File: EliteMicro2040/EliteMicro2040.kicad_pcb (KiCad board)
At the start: 2 copper layers, 17.8 x 30.5 mm, 39 parts, among them J2 B3U, U1 SPX3819M5-L-3-3, U2 Elite-C, U3 RP2040, U4 W25Q32JVSS, Y1 3225_4P

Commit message: small tweaks + generated gerbers
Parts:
- moved C2 0.37 mm to (36.1, 51.6)
- moved C1 0.22 mm to (44.4, 33.5)
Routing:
- net +3V3: track 32.2 -> 29.4 mm
- net /SWD: track 2.22 -> 0.00 mm, vias 1 -> 0
- net /SWCLK: track 1.80 -> 0.00 mm, vias 1 -> 0
- net GND: track 37.9 -> 36.5 mm
- net /GPIO4: track 4.40 -> 3.65 mm
- net /~{USB_BOOT}: track 5.20 -> 4.48 mm
- net /GPIO2: track 7.25 -> 6.65 mm
- net /GPIO17: track 7.54 -> 7.03 mm
- net /QSPI_SS: track 10.5 -> 9.99 mm, vias 1 -> 0

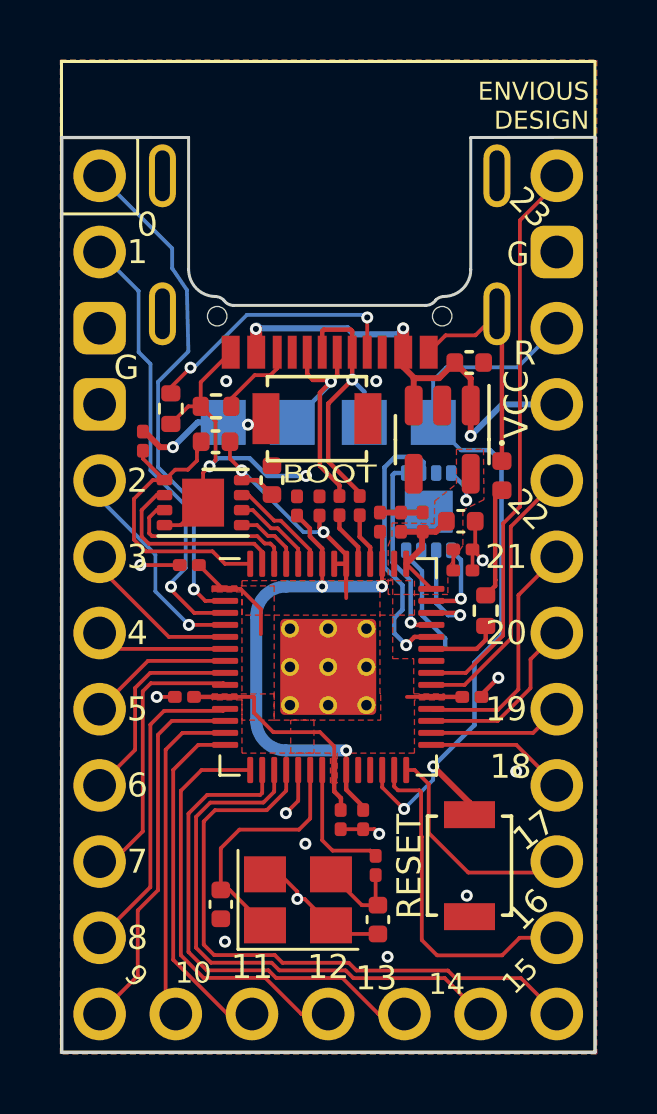
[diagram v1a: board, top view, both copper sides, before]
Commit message: matched pinout of pro-micro a bit more among various other changes.
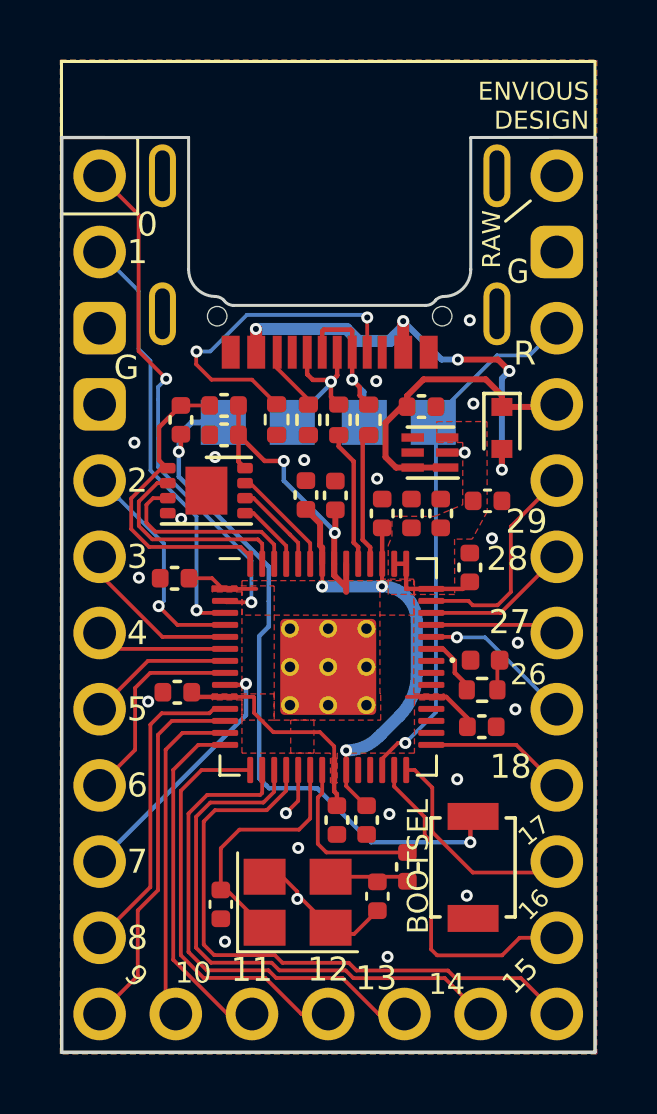
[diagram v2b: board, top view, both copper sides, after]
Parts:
- removed C9: 100nf 0201, Capacitor_SMD:C_0201_0603Metric
- removed RSW1: B3U, Button_Switch_SMD:SW_SPST_B3U-1000P
- removed U1: SPX3819M5-L-3-3, Package_TO_SOT_SMD:SOT-23-5
- removed U4: W25Q32JVSS, Package_SON:SON-8-1EP_3x2mm_P0.5mm_EP1.4x1.6mm
- added D101: 1n4002, Diode_SMD:D_SOD-523, F.Cu at (45.5, 35.7)
- added U101: TLV70033_WSON6, Package_SON:WSON-6_1.5x1.5mm_P0.5mm, F.Cu at (43.1, 36.5)
- C1: value 10uf 0402 -> 1uf 0402
- C10, C11, C13, C14, C15, C16, C18, C3, C6, C7, C8, R1, R11: footprint Capacitor_SMD:C_0201_0603Metric -> Capacitor_SMD:C_0402_1005Metric
- C4: value 10uf 0402 -> 4.7uf 0402
- R3, R4: footprint Resistor_SMD:R_0201_0603Metric -> Resistor_SMD:R_0402_1005Metric
- moved J2 15.8 mm to (44.5, 50.4), turned to -90 degrees
- moved GPIO25_LED1 6.18 mm to (44.9, 43.5), turned to 0 degrees
- moved R5 3.54 mm to (38.0, 35.4)
- moved R6 3.11 mm to (39.0, 35.4), turned to 90 degrees
- moved R4 2.88 mm to (41.0, 35.4)
- moved R3 2.86 mm to (40.0, 35.4)
- moved GPIO25_RESISTOR1 2.64 mm to (44.8, 44.4), turned to 180 degrees
- moved C5 2.20 mm to (36.2, 35.9), turned to 180 degrees
- moved C1 2.17 mm to (42.8, 35.0)
- moved R1 1.45 mm to (34.8, 35.4), turned to -90 degrees
- moved R2 1.24 mm to (36.2, 35.0)
- moved C4 1.12 mm to (45.0, 38.1)
- moved R11 1.06 mm to (42.3, 50.3)
- moved C8 1.05 mm to (44.8, 45.7)
- moved C19 0.78 mm to (41.3, 51.3)
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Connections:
- C1 pad 1: VBUS -> /VSYS
- U2 pad 17: /GPIO19 -> /GPIO26_ADC0
- U2 pad 18: /GPIO20 -> /GPIO27_ADC1
- U2 pad 19: /GPIO21 -> /GPIO28_ADC2
- U2 pad 20: /GPIO22 -> /GPIO29_ADC3
- U2 pad 21: VBUS -> /VSYS
- U2 pad 24: /GPIO23 -> unconnected-(U2-Pad24)
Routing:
- net GND: track 36.5 -> 6.34 mm, vias 16 -> 22
- net /~{USB_BOOT}: track 4.48 -> 23.9 mm
- net /GPIO23: track 18.7 -> 0.00 mm
- net /VSYS: track 0.00 -> 10.5 mm
- net /GPIO22: track 9.19 -> 0.00 mm
- net /GPIO21: track 8.10 -> 0.00 mm
- net /RUN: track 25.7 -> 19.1 mm, vias 2 -> 1
- net /GPIO20: track 5.96 -> 0.00 mm
- net /GPIO19: track 4.51 -> 0.00 mm
- net /GPIO29_ADC3: track 2.77 -> 7.24 mm, vias 1 -> 0
- net /GPIO26_ADC0: track 9.21 -> 5.18 mm
- net USB_D-: track 9.49 -> 6.01 mm
- net USB_D+: track 9.07 -> 5.71 mm
- net Net-(R4-Pad2): track 1.76 -> 4.47 mm
- net Net-(GPIO25_LED1-Pad2): track 3.73 -> 1.02 mm
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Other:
- board text added: "27"
- board text added: "28"
- board text added: "29"
- board text added: "BOOTSEL"
- board text removed: "RESET"

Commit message: modified board to fit with bastardKB's standard, added vbus sense, changed pinout, removed reset button and moved bootsel, removed SPI EEPROM as its not supported.
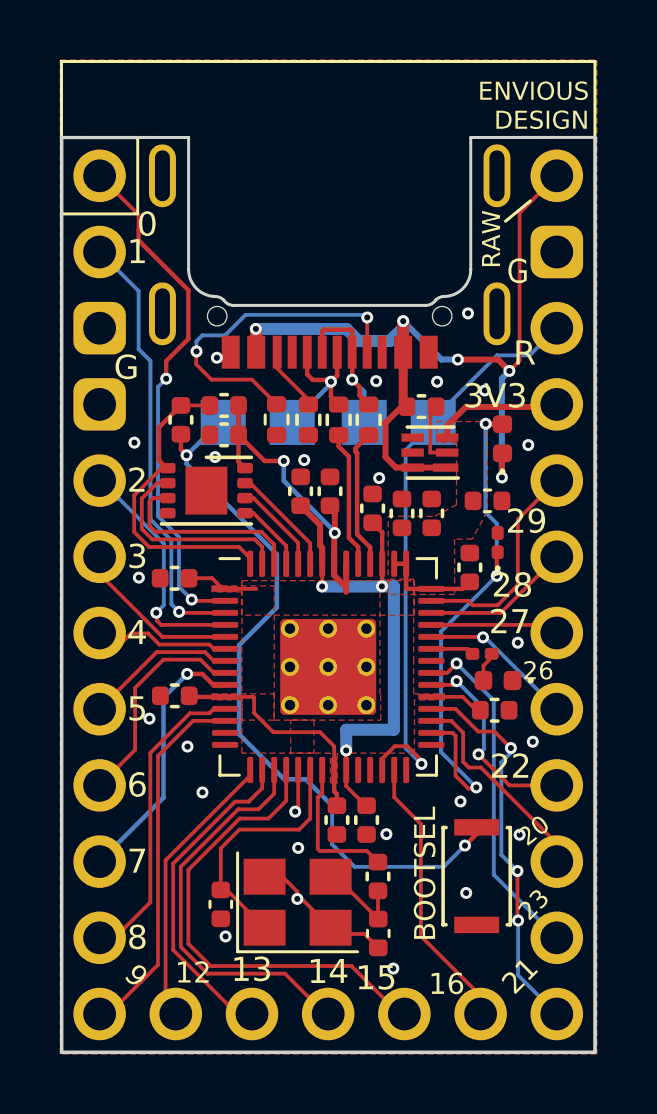
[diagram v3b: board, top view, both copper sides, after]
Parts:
- removed D101: 1n4002, Diode_SMD:D_SOD-523
- added R101: 5K6, Diode_SMD:D_0402_1005Metric, F.Cu at (45.5, 36.1)
- added R102: 0201 10K, Diode_SMD:D_0201_0603Metric, F.Cu at (45.4, 39.5)
- GPIO25_RESISTOR1: value 470 0402 Resistor -> 470 0201 Resistor; footprint Resistor_SMD:R_0402_1005Metric -> Resistor_SMD:R_0201_0603Metric
- J2: value B3U -> Button; footprint Button_Switch_SMD:SW_SPST_B3U-1000P -> Button_Switch_SMD:SW_SPST_CK_KXT3
- moved C19 1.24 mm to (41.4, 52.6)
- moved GPIO25_RESISTOR1 1.20 mm to (44.8, 43.2)
- moved R11 1.03 mm to (41.4, 50.7)
- moved GPIO25_LED1 0.80 mm to (45.4, 44.1), turned to 180 degrees
- moved C8 0.70 mm to (45.2, 45.1)
- moved C3 0.36 mm to (41.2, 38.4)
- moved C10 0.32 mm to (42.2, 38.6)
- moved J2 0.31 mm to (44.6, 50.6)
- moved C11 0.30 mm to (43.1, 38.6)
- moved C15 0.23 mm to (39.8, 37.8)
- moved C6 0.22 mm to (38.8, 37.8)
- moved C14 0.14 mm to (34.6, 44.6)
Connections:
- C1 pad 1: /VSYS -> VBUS
- U101 pad 1: /VSYS -> VBUS
- U101 pad 6: /VSYS -> VBUS
- U2 pad 13: /GPIO15 -> /GPIO21
- U2 pad 14: /GPIO16 -> /GPIO23
- U2 pad 15: /GPIO17 -> /GPIO20
- U2 pad 16: /GPIO18 -> /GPIO22
- U2 pad 21: /VSYS -> +3V3
- U2 pad 24: unconnected-(U2-Pad24) -> VBUS
- U2 pad 25: /GPIO10 -> /GPIO12
- U2 pad 26: /GPIO11 -> /GPIO13
- U2 pad 27: /GPIO12 -> /GPIO14
- U2 pad 28: /GPIO13 -> /GPIO15
- U2 pad 29: /GPIO14 -> /GPIO16
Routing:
- net /GPIO19: track 0.00 -> 18.0 mm, vias 0 -> 3
- net VBUS: track 16.3 -> 29.6 mm
- net /GPIO21: track 0.00 -> 13.0 mm, vias 0 -> 3
- net /GPIO11: track 11.8 -> 0.00 mm
- net /GPIO23: track 0.00 -> 11.5 mm, vias 0 -> 1
- net /GPIO10: track 10.7 -> 0.00 mm
- net /VSYS: track 10.5 -> 0.00 mm
- net /GPIO17: track 6.94 -> 0.00 mm
- net /GPIO22: track 0.00 -> 6.82 mm, vias 0 -> 2
- net /GPIO20: track 0.00 -> 6.44 mm
- net /GPIO13: track 16.2 -> 10.3 mm
- net /GPIO14: track 18.4 -> 13.3 mm
- net /GPIO12: track 13.8 -> 8.77 mm
- net /GPIO15: track 20.7 -> 15.7 mm
- net /GPIO18: track 4.74 -> 0.00 mm
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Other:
- board text added: "3V3"

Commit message: lots of changes, swapped many parts to 0402, swapped SOT regulator to small WSON, made sure there is proper parity between footprint and value, etc etc etc
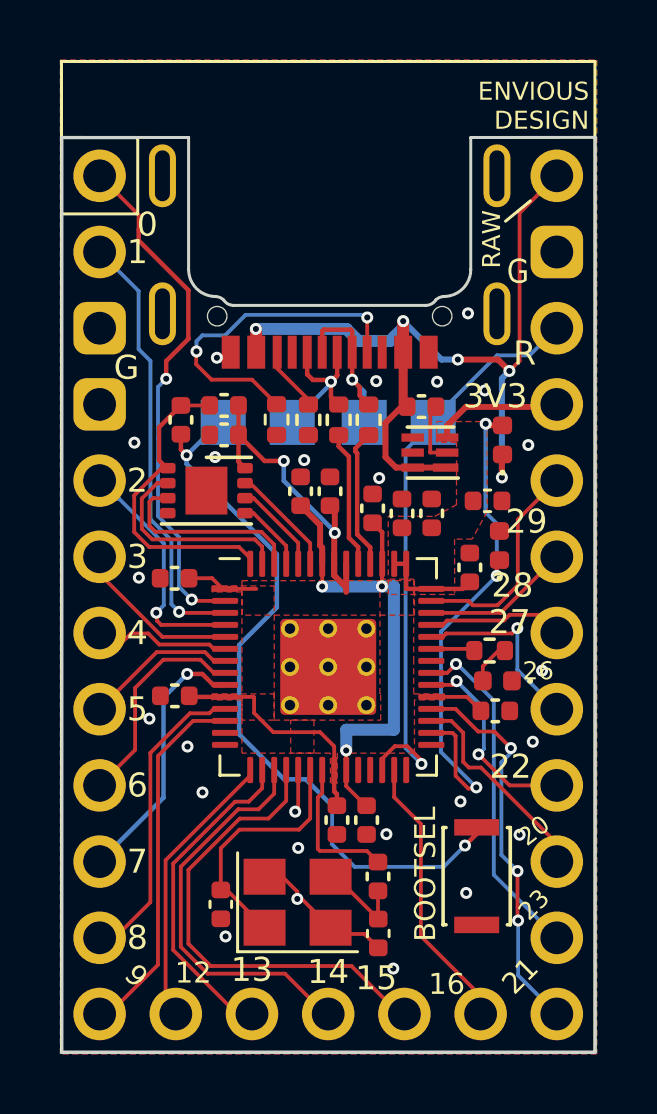
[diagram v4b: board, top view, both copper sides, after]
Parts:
- C10, C3: value 1uf 0201 -> 1uf 0402
- C11, C13, C14, C15, C16, C18, C6, C7, C8: value 100nf 0201 -> 100nf 0402
- GPIO25_RESISTOR1: footprint Resistor_SMD:R_0201_0603Metric -> Resistor_SMD:R_0402_1005Metric
- R102: footprint Diode_SMD:D_0201_0603Metric -> Diode_SMD:D_0402_1005Metric
- moved GPIO25_RESISTOR1 0.27 mm to (45.1, 43.1)
- moved R102 0.11 mm to (45.4, 39.6)
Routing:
- net /GPIO26_ADC0: track 5.18 -> 6.23 mm
- net Net-(GPIO25_LED1-Pad2): track 0.89 -> 1.44 mm

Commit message: made some smaller components generated new gerber
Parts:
- GPIO25_RESISTOR1: value 470 0201 Resistor -> 470 0402 Resistor
- R1, R11: value 1K 0201 Resistor -> 1K 402 Resistor
- R101: value 5K6 -> 5.6k 0402; footprint Diode_SMD:D_0402_1005Metric -> Resistor_SMD:R_0402_1005Metric
- R102: value 0201 10K -> 10k 0402; footprint Diode_SMD:D_0402_1005Metric -> Resistor_SMD:R_0402_1005Metric
- R3, R4: value 27 0201 -> 27 0402
- U101: value TLV70033_WSON6 -> TLV70033
- Y1: value 3225_4P -> 2520_4P 12Mhz; footprint Crystal:Crystal_SMD_3225-4Pin_3.2x2.5mm -> Crystal:Crystal_SMD_2520-4Pin_2.5x2.0mm
- moved C19 0.42 mm to (41.0, 52.6)
- moved R11 0.41 mm to (41.0, 50.7)
- moved C2 0.33 mm to (36.5, 51.6)
- moved C3 0.32 mm to (41.5, 38.6)
- moved C10 0.26 mm to (42.4, 38.6)
- moved C11 0.25 mm to (43.4, 38.6)
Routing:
- net GND: track 7.57 -> 4.60 mm, vias 25 -> 24
- net XIN: track 8.18 -> 7.57 mm
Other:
- rule pad_to_mask_clearance: 0.051 -> 0

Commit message: preparation for order.
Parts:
- removed TP3: TestPoint, EnvExtras:CustomTestPoint
- added TP101: TestPoint, EnvExtras:CustomTestPoint, B.Cu at (39.7, 51.7)
- added TP102: TestPoint, EnvExtras:CustomTestPoint, B.Cu at (42.7, 51.7)
- added TP103: TestPoint, EnvExtras:CustomTestPoint, B.Cu at (36.7, 51.7)
- FLASH1: value W25Q16FWUXIE -> W25Q16JVUXIQ
- moved TP1 1.20 mm to (39.7, 35.5)
- moved TP2 1.20 mm to (42.1, 35.5)
- moved TP4 1.20 mm to (37.4, 35.5)
- moved C2 0.81 mm to (35.7, 51.9)
- moved C19 0.75 mm to (40.2, 52.6)
- moved R11 0.75 mm to (40.2, 50.7)
- moved Y1 0.69 mm to (38.0, 51.4)
- moved C7 0.63 mm to (41.2, 49.4)
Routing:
- net /SWD: track 0.00 -> 11.8 mm, vias 0 -> 1
- net /SWCLK: track 0.00 -> 7.25 mm, vias 0 -> 1
- net GND: track 4.60 -> 11.5 mm, vias 24 -> 25
- net XIN: track 7.57 -> 8.59 mm
- net +1V1: track 17.4 -> 18.2 mm
- net XOUT: track 4.49 -> 3.74 mm
- net /~{USB_BOOT}: track 24.6 -> 23.9 mm
- net USB_D+: track 5.71 -> 5.08 mm
- net Net-(C19-Pad2): track 2.80 -> 3.30 mm
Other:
- board text added: "G"
- board text added: "SWC"
- board text added: "SWD"
- board text removed: "RUN"

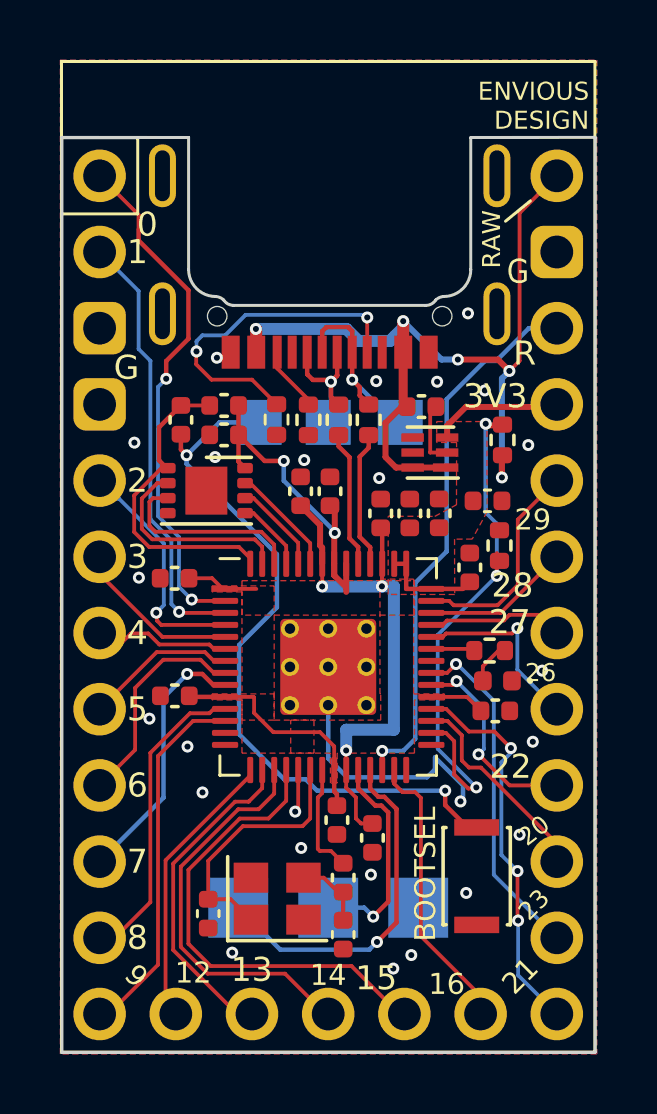
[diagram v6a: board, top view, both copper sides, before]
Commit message: added diode after VBUS to make sure VBUS Detect can work properly.
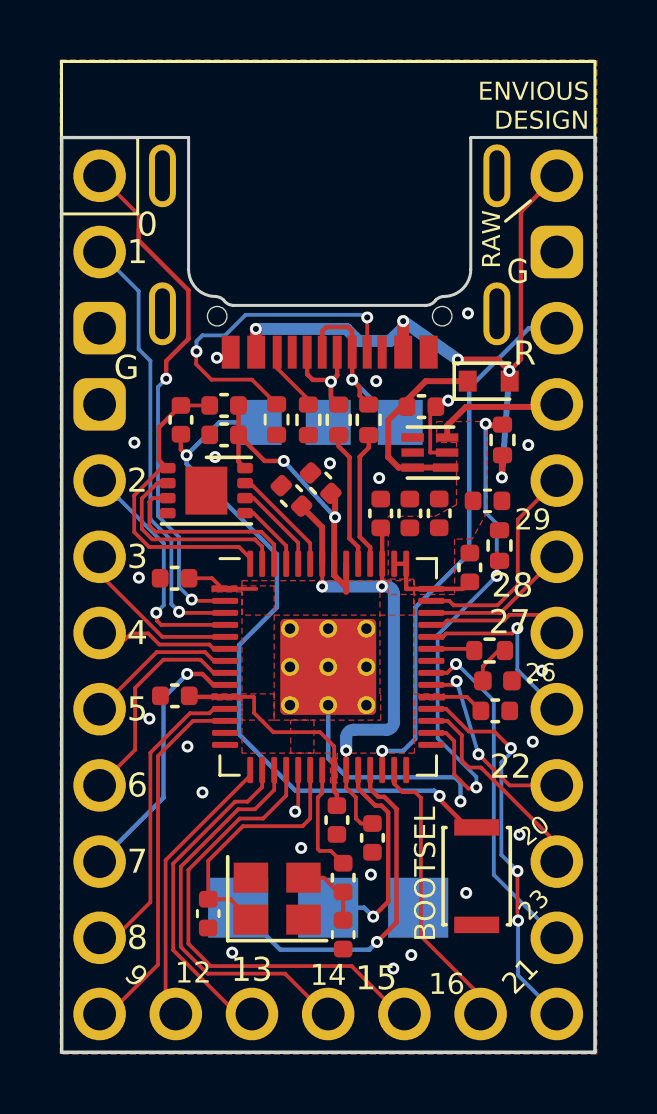
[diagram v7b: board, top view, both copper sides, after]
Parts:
- added D1: Schottky Barrier SOD-523, Diode_SMD:D_SOD-523, F.Cu at (45.0, 34.1)
- moved C15 0.41 mm to (39.5, 37.5), turned to 135 degrees
- moved C6 0.34 mm to (38.5, 38.0), turned to 135 degrees
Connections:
- C1 pad 1: VBUS -> VSYS
- U101 pad 1: VBUS -> VSYS
- U101 pad 6: VBUS -> VSYS
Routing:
- net VSYS: track 0.00 -> 6.62 mm
- net VBUS: track 29.6 -> 23.6 mm
- net GND: track 11.5 -> 10.7 mm, vias 25 -> 24
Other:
- board text removed: "3V3"

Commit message: made various improvements to design such as swapping vbus for vsys on the raw pin
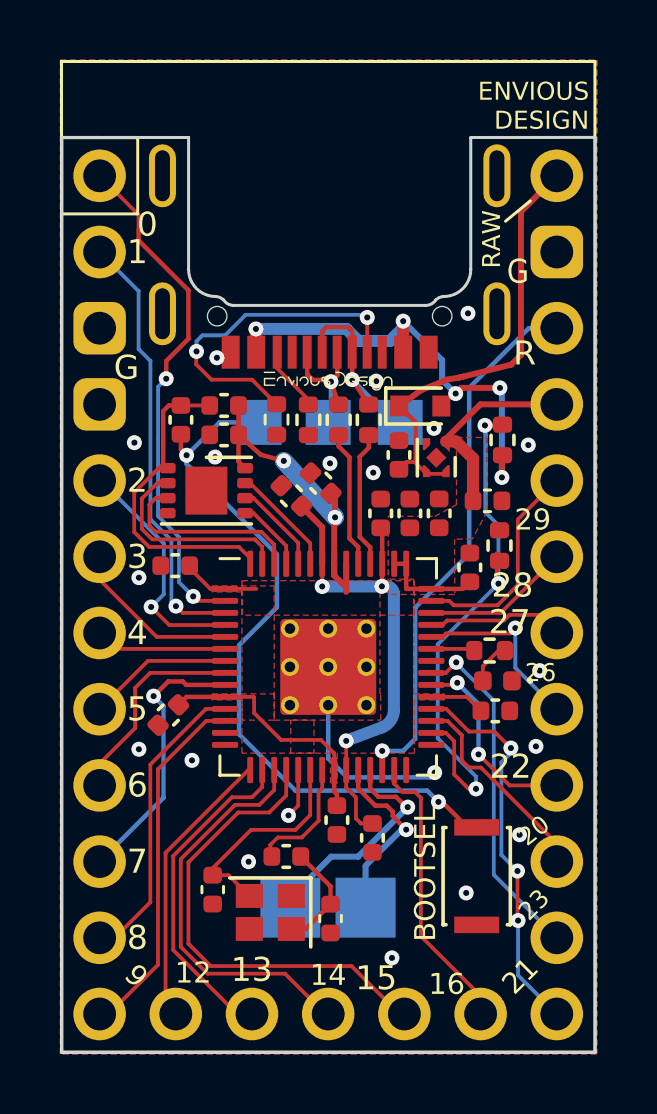
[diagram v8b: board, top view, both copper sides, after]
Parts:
- removed R11: 1K 402 Resistor, Capacitor_SMD:C_0402_1005Metric
- removed TP102: TestPoint, EnvExtras:CustomTestPoint
- added G***: LOGO, EnvExtras:pattern, B.Cu at (39.7, 53.8)
- added R7: 1K 0402, Capacitor_SMD:C_0402_1005Metric, F.Cu at (38.3, 50.0)
- added kibuzzard-63496A2F: G***, kibuzzard-63496A2F, F.Cu at (39.7, 34.1)
- C2: value 22pf 0402 -> 22pF 0402
- D1: value Schottky Barrier SOD-523 -> Schottky Barrier SOD-723
- U101: value TLV70033 -> WL2810D33-4/TR; footprint Package_SON:WSON-6_1.5x1.5mm_P0.5mm -> Package_DFN_QFN:UDFN-4-1EP_1x1mm_P0.65mm_EP0.48x0.48mm
- Y1: value 2520_4P 12Mhz -> 2016_4P; footprint Crystal:Crystal_SMD_2520-4Pin_2.5x2.0mm -> Crystal:Crystal_SMD_2016-4Pin_2.0x1.6mm
- moved C19 4.60 mm to (35.9, 51.1), turned to -90 degrees
- moved C2 4.08 mm to (39.8, 52.1), turned to -90 degrees
- moved D1 2.43 mm to (42.8, 35.0)
- moved C1 1.78 mm to (42.1, 36.6), turned to 90 degrees
- moved TP103 1.74 mm to (38.4, 51.7)
- moved TP101 1.25 mm to (40.9, 51.7)
- moved C14 0.68 mm to (34.4, 45.3), turned to -135 degrees
- moved Y1 0.51 mm to (37.8, 51.9), turned to 180 degrees
- moved C16 0.42 mm to (34.6, 40.3)
- moved U101 0.27 mm to (43.3, 36.7), turned to -90 degrees
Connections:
- C19 pad 1: GND -> Net-(C19-Pad1)
- C19 pad 2: Net-(C19-Pad2) -> GND
- C2 pad 1: GND -> Net-(C2-Pad1)
- C2 pad 2: XIN -> GND
- U101 pad 1: VSYS -> +3V3
- U101 pad 3: +3V3 -> VSYS
- U101 pad 4: unconnected-(U101-Pad4) -> VSYS
- U2 pad 24: VBUS -> VSYS
- U3 pad 20: XIN -> Net-(C19-Pad1)
- U3 pad 21: XOUT -> Net-(R7-Pad2)
- Y1 pad 1: XIN -> GND
- Y1 pad 2: GND -> Net-(C19-Pad1)
- Y1 pad 3: Net-(C19-Pad2) -> GND
- Y1 pad 4: GND -> Net-(C2-Pad1)
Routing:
- net XIN: track 8.59 -> 0.00 mm
- net VSYS: track 6.62 -> 14.9 mm
- net Net-(C19-Pad1): track 0.00 -> 7.23 mm
- net VBUS: track 23.6 -> 16.5 mm
- net /SWD: track 11.8 -> 7.63 mm
- net Net-(R7-Pad2): track 0.00 -> 4.02 mm
- net +3V3: track 29.6 -> 33.5 mm
- net XOUT: track 3.74 -> 0.00 mm
- net Net-(C2-Pad1): track 0.00 -> 3.65 mm
- net GND: track 10.7 -> 7.30 mm, vias 24 -> 20
- net Net-(C19-Pad2): track 3.30 -> 0.00 mm
- net +1V1: track 17.8 -> 16.6 mm
- net /SWCLK: track 7.25 -> 6.12 mm
